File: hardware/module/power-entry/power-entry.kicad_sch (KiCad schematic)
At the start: 19 parts

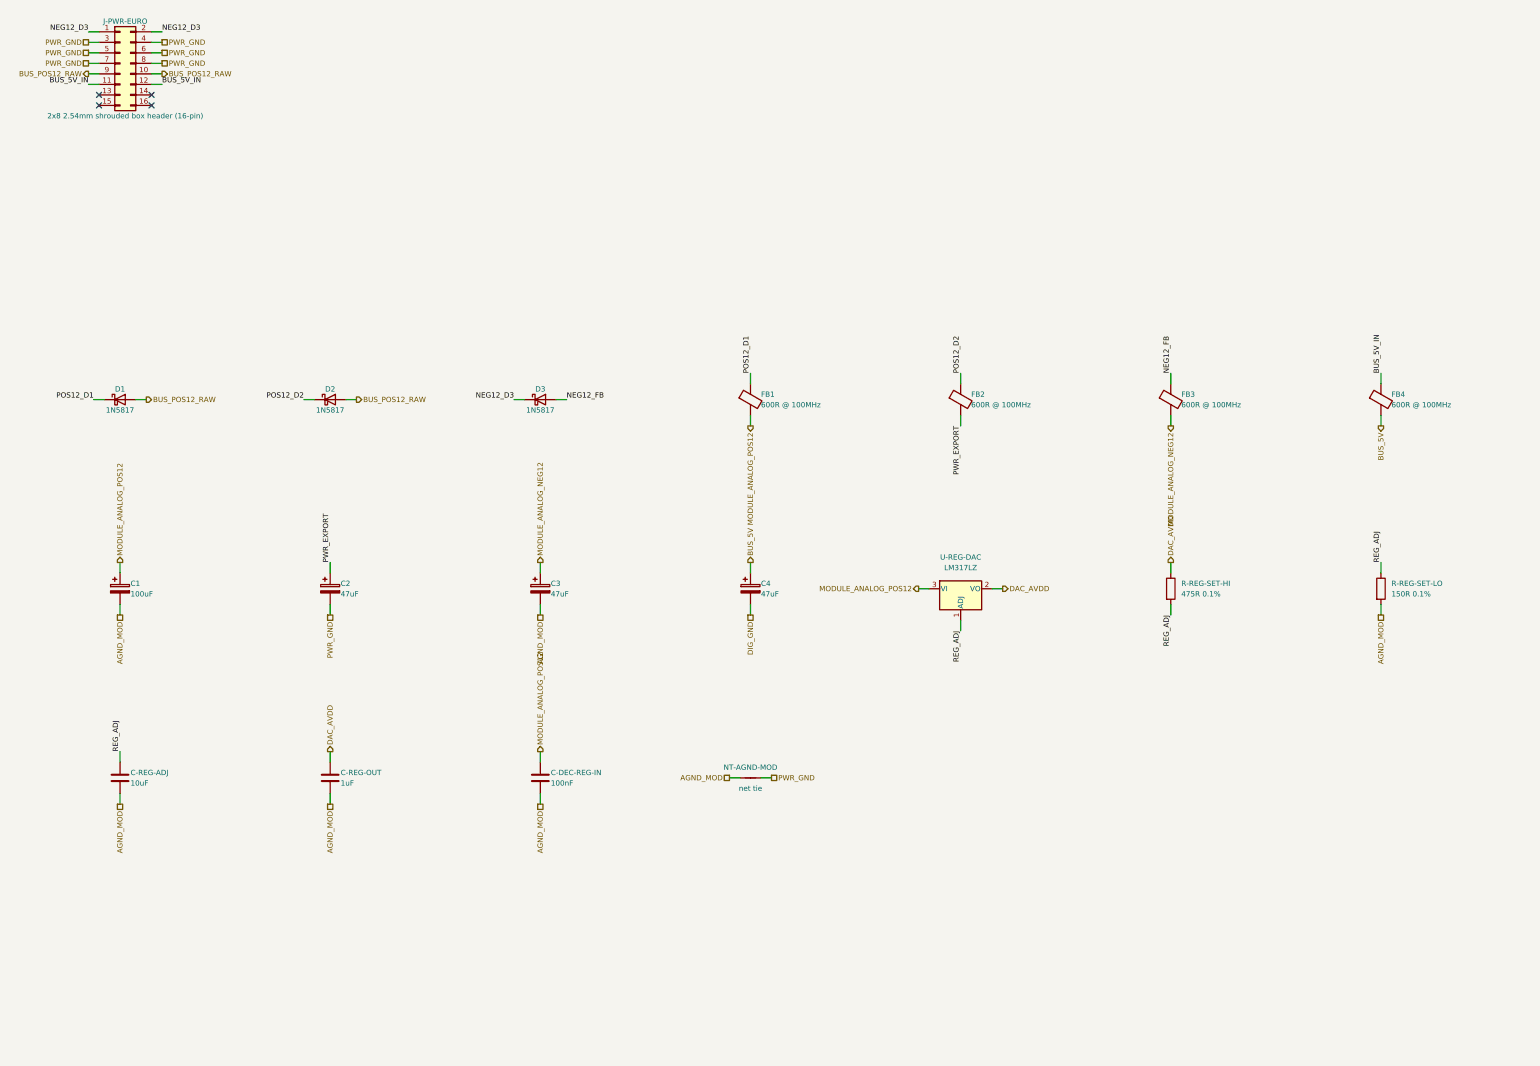
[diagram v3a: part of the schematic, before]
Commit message: Module: four-layer ground settled, local 5 V, metal standoffs, pitch budget, board-to-board header
Owner decisions of 2026-09-30 applied. dig-gnd-topology settled: one star at
J-PWR-EURO's ground pins, DIG_GND a layer-2 plane tied there by the new
NT-DIG-MOD, AGND_MOD its own region by NT-AGND-MOD, PWR_GND on layer 4; the
proposal's bridge under the DAC dropped per SBAS430E p.49 (DIG_GND was an
island tied only through the cable before). PCB-MODULE four layers, the jack
board two. The bus +5 V is not used: U-REG-LOGIC (ADP7118AUJZ-5.0, banked)
makes LOGIC_5V from the analog +12 V; FB4/C4 gone, the 16-pin header kept
with its +5 V/CV/Gate pins no-connect (ADR 0023 point 3 amended). Metal
standoffs: pads AGND_MOD on the jack board, no net on the main board.
pitch-cents-budget settled at 0.76 cents linear / 0.45 RSS from one table.
J-B2B-MOD is Samtec TSW-110-09-G-D. Module sims are stale and re-run next.

Co-Authored-By: Claude Opus 5.5 <noreply@anthropic.com>
Claude-Session: https://claude.ai/code/session_01LmB4muFXnoLprWX4JzuJ5A
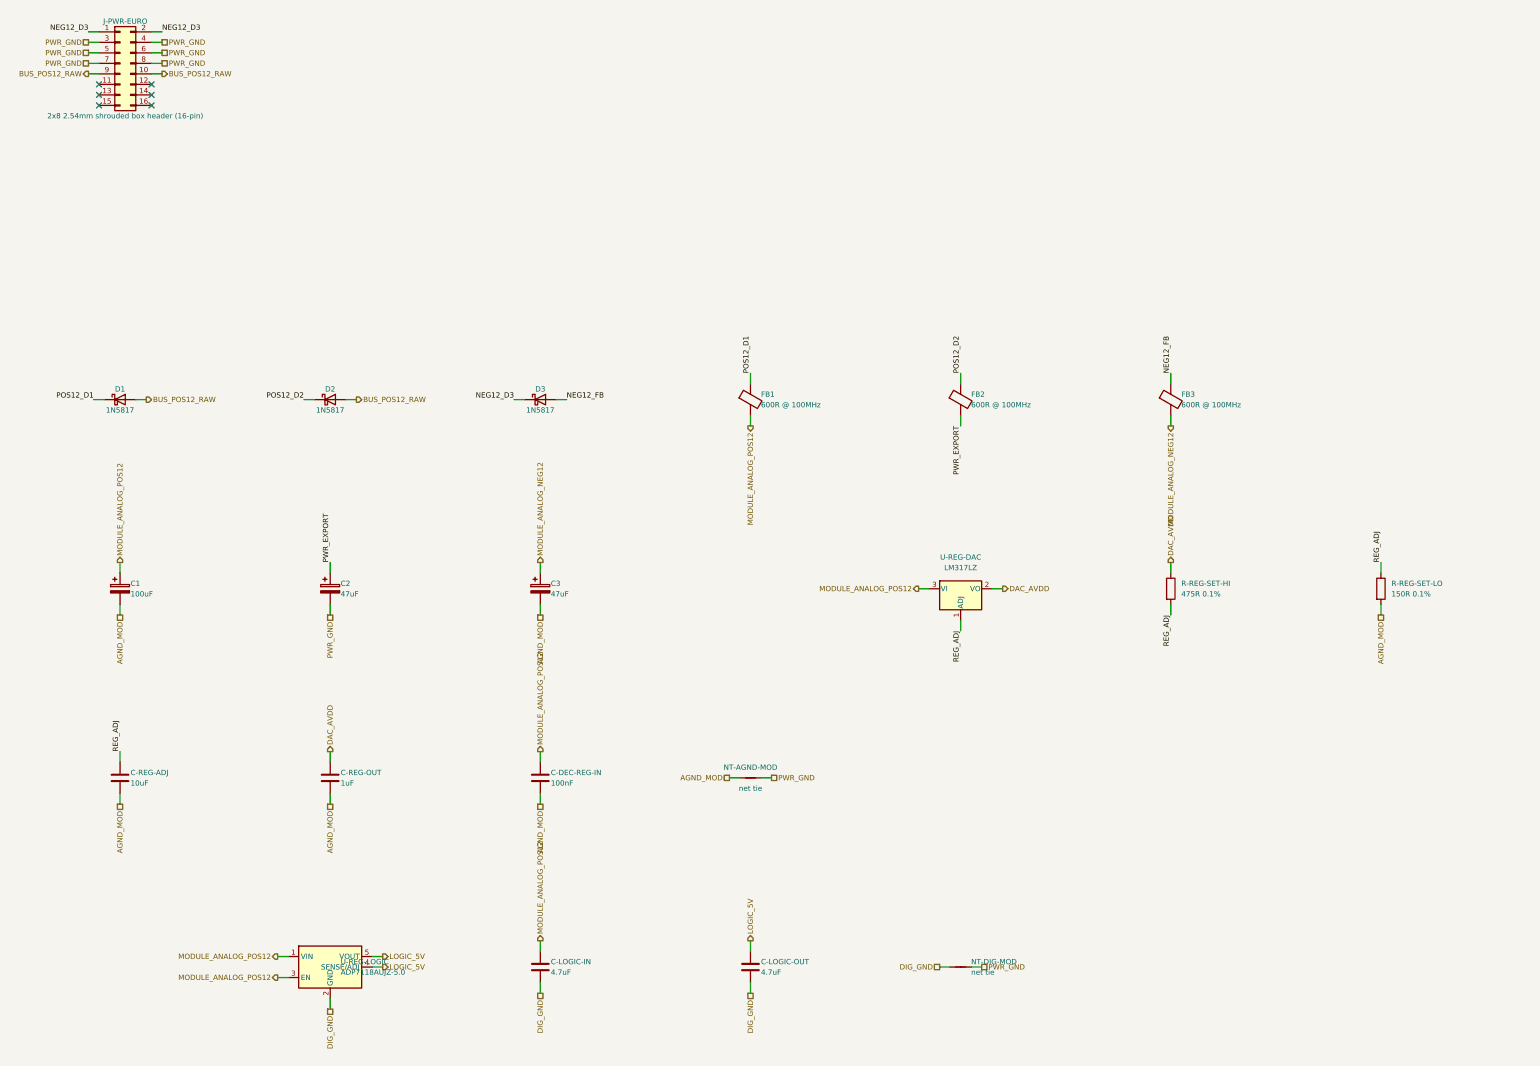
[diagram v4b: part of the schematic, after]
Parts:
- removed C4: 47uF, Capacitor_THT:CP_Radial_D5.0mm_P2.00mm, symbol Device:C_Polarized
- removed FB4: 600R @ 100MHz, Inductor_SMD:L_1206_3216Metric, symbol Device:FerriteBead
- added C-LOGIC-IN, C-LOGIC-OUT: 4.7uF, Capacitor_SMD:C_1206_3216Metric, symbol Device:C
- added NT-DIG-MOD: net tie, NetTie:NetTie-2_SMD_Pad0.5mm, symbol Device:NetTie_2
- added U-REG-LOGIC: ADP7118AUJZ-5.0, Package_TO_SOT_SMD:TSOT-23-5, symbol Regulator_Linear:ADP7142AUJZ
- J-PWR-EURO: Note Keyed, but a key does not make a reversed ribbon impossible. The rack's -12 V is the pin-1 pair, the ribbon's red stripe, and reversing it is what D-REVPOL exists for -> Keyed, but a key does not make a reversed ribbon impossible. The rack's -12 V is the pin-1 pair, the ribbon's red stripe, and reversing it is what D-REVPOL exists for. The bus +5 V (11, 12) and CV/Gate (13-16) pins are NOT USED: pads present, no-connect - the module makes its own 5 V (U-REG-LOGIC), and the header stays 2x8 for commonality with every Eurorack power cable (owner, 2026-09-30)
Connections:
- net DIG_GND: now also C-LOGIC-IN.2, C-LOGIC-OUT.2, NT-DIG-MOD.1, U-REG-LOGIC.2 (GND)
- net MODULE_ANALOG_POS12: now also C-LOGIC-IN.1, U-REG-LOGIC.1 (VIN), U-REG-LOGIC.3 (EN)
- net PWR_GND: now also NT-DIG-MOD.2
- net BUS_5V_IN: no longer names the net of J-PWR-EURO.11 (Pin_11)
- net BUS_5V_IN: no longer J-PWR-EURO.12 (Pin_12)
- new net LOGIC_5V: C-LOGIC-OUT.1, U-REG-LOGIC.4 (SENSE/ADJ), U-REG-LOGIC.5 (VOUT)
- no-connect marks 4 -> 6

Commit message: WIP module power entry: rail PTCs, the instrument's isolated supply (U-ISO), ground split
Sheets, exports, BOM rows, banked datasheets (manifest fragment to follow).
The page drawing, ADR 0027, figures and sims are the next commits.

Co-Authored-By: Claude Opus 5.5 <noreply@anthropic.com>
Claude-Session: https://claude.ai/code/session_01LmB4muFXnoLprWX4JzuJ5A
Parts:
- added C-ISO-IN: 4.7uF 50V, Capacitor_SMD:C_1206_3216Metric, symbol Device:C
- added C-ISO-OUT: 100uF 25V, Capacitor_SMD:CP_Elec_6.3x5.8, symbol Device:C_Polarized
- added C-ISO-Y: 1nF, Capacitor_SMD:C_0805_2012Metric, symbol Device:C
- added D4: 1N5817, Diode_THT:D_DO-41_SOD81_P10.16mm_Horizontal, symbol Diode:1N5817
- added FB4: 600R @ 100MHz, Inductor_SMD:L_1206_3216Metric, symbol Device:FerriteBead
- added L-ISO-IN: 22uH, Inductor_SMD:L_Sunlord_SWPA6028S, symbol Device:L
- added NT-UMB-MOD: net tie, NetTie:NetTie-2_SMD_Pad0.5mm, symbol Device:NetTie_2
- added PTC-ISO: MF-MSMF075/33X-2, Fuse:Fuse_1812_4532Metric, symbol Device:Polyfuse
- added PTC-NEG12, PTC-POS12: MF-MSMF020/60-2, Fuse:Fuse_1812_4532Metric, symbol Device:Polyfuse
- added U-ISO: URB2412YMD-15WR3, woody:Converter_DCDC_Mornsun_URB_YMD-15WR3_THT, symbol woody:URB_YMD-15WR3
- C2: value 47uF -> 100uF 50V; footprint Capacitor_THT:CP_Radial_D5.0mm_P2.00mm -> Capacitor_SMD:CP_Elec_6.3x7.7; LCSC C371230 -> (none); MPN NXB25V47M5*11 2.5TP -> UCM1H101MCL1GS; Manufacturer SamYoung -> Nichicon; Note (none) -> U-ISO's input bulk, ACROSS its input (ISO_VIN_POS to ISO_VI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; Row C-BULK-RAIL -> C-ISO-BULK
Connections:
- net BUS_POS12_RAW: now also PTC-ISO.1, PTC-POS12.1; no longer D1.2 (A), D2.2 (A)
- net DIG_GND: now also NT-UMB-MOD.2
- net PWR_GND: now also C-ISO-OUT.2, C-ISO-Y.2, NT-UMB-MOD.1, U-ISO.6 (0V); no longer C2.2, J-PWR-EURO.3 (Pin_3), J-PWR-EURO.4 (Pin_4), J-PWR-EURO.5 (Pin_5), J-PWR-EURO.6 (Pin_6), J-PWR-EURO.7 (Pin_7), J-PWR-EURO.8 (Pin_8), NT-AGND-MOD.2, NT-DIG-MOD.2
- net NEG12_D3 renamed BUS_NEG12_RAW
- net BUS_NEG12_RAW: now also D4.1 (K), PTC-NEG12.1; no longer D3.1 (K)
- net PWR_EXPORT renamed ISO_FB2
- net ISO_FB2: now also L-ISO-IN.1; no longer C2.1
- new net BUS_GND: J-PWR-EURO.3 (Pin_3), J-PWR-EURO.4 (Pin_4), J-PWR-EURO.5 (Pin_5), J-PWR-EURO.6 (Pin_6), J-PWR-EURO.7 (Pin_7), J-PWR-EURO.8 (Pin_8), NT-AGND-MOD.2, NT-DIG-MOD.2
- new net ISO_POS12: C-ISO-OUT.1, U-ISO.4 (+Vo)
- new net ISO_VIN_NEG: C-ISO-IN.2, C2.2, FB4.2, U-ISO.2 (GND)
- new net ISO_VIN_POS: C-ISO-IN.1, C-ISO-Y.1, C2.1, L-ISO-IN.2, U-ISO.3 (Vin)
- new net NEG12_D4: D4.2 (A), FB4.1
- new net NEG12_PTC3: D3.1 (K), PTC-NEG12.2
- new net POS12_PTC1: D1.2 (A), PTC-POS12.2
- new net POS12_PTC2: D2.2 (A), PTC-ISO.2
- no-connect marks 6 -> 8
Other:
- note added: "ADDED 2026-09-30 (ADR 0027): the rail fuses (PTC-POS12, PTC-NEG12), the instrument's isolated supply - PTC-ISO, D2, FB2, L-ISO-IN on the +12 leg, D4, FB4 on the -12 leg, C2 and C-ISO-IN across, U-ISO, C-ISO-OUT, C-ISO-Y - and NT-UMB-MOD. BUS_GND is the Eurorack ground as it arrives, the star: AGND_MOD (NT-AGND-MOD) and DIG_GND (NT-DIG-MOD) meet it, and PWR_GND - U-ISO's isolated return - meets DI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"

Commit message: ADR 0027 follow-through: load switch page and sheet on ISO_POS12, ADR 0004/0005 amendments, sims re-run, renders
The load switch page states its new supply and the margins it gains (ON
turn-on 0.94 V below U-ISO's floor, was 0.7 V below the bus's); sheet notes
and text follow; the power-entry sheet no longer declares foreign parts its
drawing stopped showing. ADR 0004 and 0005 carry dated amendments pointing
at ADR 0027; pitch-stage.md's exclusion reads as removed. Sim READMEs record
the ground-shift decks and the LM317L model's non-convergence at the fuse's
post-trip 6 ohm. All gates pass; sims re-run on the final netlists.

Co-Authored-By: Claude Opus 5.5 <noreply@anthropic.com>
Claude-Session: https://claude.ai/code/session_01LmB4muFXnoLprWX4JzuJ5A
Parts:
- C1: Note 100uF on +12 V, NOT 47uF - the other three are 47uF and thi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 -> 100uF on +12 V, NOT 47uF - C3 on -12 V is 47uF and this one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
- D2: Note Reverse protection, EXPORTED +12 V branch. Separate from D1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 -> Reverse protection, the +12 V leg of U-ISO's input (ADR 002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
- D3: Note Reverse protection, -12 V branch. CATHODE TO THE BUS, anode to the module's -12 V rail: the rail's current flows out of the module into the bus's -12 V, so this is the one entry diode the other way round from D1/D2 -> Reverse protection, -12 V branch. CATHODE TO THE BUS, anode to the module's -12 V rail: the rail's current flows out of the module into the bus's -12 V, so this is, with D4, the entry diode the other way round from D1/D2
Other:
- note added: "ADDED 2026-09-30 (ADR 0027): the rail fuses (PTC-POS12, PTC-NEG12), the instrument's isolated supply - PTC- ISO, D2, FB2, L-ISO-IN on the +12 leg, D4, FB4 on the -12 leg, C2 and C-ISO-IN across, U-ISO, C-ISO-OUT, C-ISO-Y - and NT-UMB-MOD. BUS_GND is the Eurorack ground as it arrives, the star: AGND_MOD (NT-AGND-MOD) and DIG_GND (NT-DIG-MOD) meet it, and PWR_GND - U-ISO's isolated return - meets D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"
- note added: "FROM THE HAND-WRITTEN NETLIST THIS SHEET REPLACES (verbatim; the part notes are on each part's Note field): AUTHORITATIVE for connectivity. The drawing in power-entry.md is a representation of this file. SCOPE. This circuit owns the rail entry and its fuses, the bead-and-bulk branches, the LM317, the logic 5 V and the instrument's isolated supply up to ISO_POS12 and PWR_GND. The load switch those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"
- note removed: "ADDED 2026-09-30 (ADR 0027): the rail fuses (PTC-POS12, PTC-NEG12), the instrument's isolated supply - PTC-ISO, D2, FB2, L-ISO-IN on the +12 leg, D4, FB4 on the -12 leg, C2 and C-ISO-IN across, U-ISO, C-ISO-OUT, C-ISO-Y - and NT-UMB-MOD. BUS_GND is the Eurorack ground as it arrives, the star: AGND_MOD (NT-AGND-MOD) and DIG_GND (NT-DIG-MOD) meet it, and PWR_GND - U-ISO's isolated return - meets DI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"
- note removed: "FROM THE HAND-WRITTEN NETLIST THIS SHEET REPLACES (verbatim; the part notes are on each part's Note field): AUTHORITATIVE for connectivity. The drawing in power-entry.md is a representation of this file. SCOPE. That drawing shows the whole load switch - LT1641, R-ILIM, the timer and gate capacitors, the FB divider and Q-LOADSW - so the export path can be read in one place. THOSE ARE module/umbili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"
- note removed: "PARTS THIS PAGE'S DRAWING SHOWS AND THIS CIRCUIT DOES NOT OWN - netlist.yaml `foreign:`, exported from the FOREIGN lines below. Each is counted, netted and ordered by its owner; declaring it keeps the drawing checkable (tools/check-netlist.py). FOREIGN R-ILIM: owner module/umbilical-load-switch, row R-ILIM FOREIGN R-GATE-SER: owner module/umbilical-load-switch, row R-GATE-SER FOREIGN R-GATE-COMP: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"

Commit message: U-ISO becomes RECOM RP20-2412SAW: footprint, symbol, sheet, BOM rows
Same land pattern as the MORNSUN part, RECOM's pin numbers; the plain SAW
has no CTRL or Trim pin, so pads 1/2/4/6 and no no-connects. Filter parts'
provenance moved to the RECOM datasheet; PTC-ISO is RECOM's required
input fuse. Page and ADR follow in the next commit.

Co-Authored-By: Claude Opus 5.5 <noreply@anthropic.com>
Claude-Session: https://claude.ai/code/session_01LmB4muFXnoLprWX4JzuJ5A
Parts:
- C-ISO-IN: Note Across U-ISO's input pins, beside them: the ceramic half of the input filter (the datasheet's C1/C2, 4.7uF/50V, p.5 Fig.3) -> Across U-ISO's input pins, beside them: the ceramic half of the input filter (RECOM's Class B C1 for the RP20-24xxSAW, 4.7uF MLCC, PD-6; 50 V here because it sits across both rails)
- C-ISO-OUT: Note U-ISO's output capacitor, the datasheet's Cout 100uF/25V (p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 -> U-ISO's output capacitor, 100uF/25V: well inside the RP20-2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
- C-ISO-Y: Note Across the isolation barrier AT the converter, ISO_VIN_POS to PWR_GND: gives the switching common-mode current a 1 nF path home beside U-ISO instead of round the star and the ribbon (the datasheet's CY, p.5 Fig.3). On the +12 V side so PTC-ISO covers it if it fails short -> Across the isolation barrier AT the converter, ISO_VIN_POS to PWR_GND: gives the switching common-mode current a 1 nF path home beside U-ISO instead of round the star and the ribbon (RECOM's Class B filter puts 470pF across the barrier on each side, C4/C5, PD-6; one 1 nF here). On the +12 V side so PTC-ISO covers it if it fails short
- C2: Note U-ISO's input bulk, ACROSS its input (ISO_VIN_POS to ISO_VIN_NEG, 24 V): the datasheet's Cin, 100uF/50V (MORNSUN-URB_YMD-15WR3.pdf p.4 Fig.2). An electrolytic with real ESR, because it damps L-ISO-IN (power-entry.md) -> U-ISO's input bulk, ACROSS its input (ISO_VIN_POS to ISO_VIN_NEG, 24 V): the external input electrolytic RECOM asks for (RECOM-RP20-AW.pdf PD-5 Note 11, which suggests 220uF/100V where a surge test applies; 100uF/50V here, on the rack's rails). An electrolytic with real ESR, because it damps L-ISO-IN (power-entry.md)
- PTC-ISO: Note The converter branch's fuse, in its +12 V leg ahead of D2: 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 -> The converter branch's fuse, in its +12 V leg ahead of D2, 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
- U-ISO: value URB2412YMD-15WR3 -> RP20-2412SAW; footprint woody:Converter_DCDC_Mornsun_URB_YMD-15WR3_THT -> woody:Converter_DCDC_RECOM_RP20-xxxxSAW_THT; symbol woody:URB_YMD-15WR3 -> woody:RP20-xxxxSAW; MPN URB2412YMD-15WR3 -> RP20-2412SAW; Manufacturer MORNSUN -> RECOM; Note THE INSTRUMENT'S SUPPLY, ISOLATED (ADR 0027): input across the rack's +12 V and -12 V, so the instrument's current loops rail to rail and never enters the rack's ground; output +12 V to the load switch, return on PWR_GND, which meets the module's grounds only through NT-UMB-MOD and NT-DIG-MOD. Ctrl open = on, Trim open = 12 V (p.2, p.5) -> THE INSTRUMENT'S SUPPLY, ISOLATED (ADR 0027): input across the rack's +12 V and -12 V, so the instrument's current loops rail to rail and never enters the rack's ground; output +12 V to the load switch, return on PWR_GND, which meets the module's grounds only through NT-UMB-MOD and NT-DIG-MOD. The standard RP20-2412SAW has no CTRL and no Trim pin (PD-1 Note 3): always on, 12 V nominal. RECOM requires an input fuse (PD-4 Note 8): PTC-ISO; Pins CTRL=1(Ctrl) GND=2(GND) VIN=3(Vin) VO=4(+Vo) TRIM=5(Trim) 0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 -> VIN=1(+Vin) GND=2(-Vin) VO=4(+Vout) 0V=6(-Vout); Pins_source datasheets/discrete-and-power/MORNSUN-URB_YMD-15WR3.pdf p.6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 -> datasheets/discrete-and-power/RECOM-RP20-AW.pdf PD-6 Pinnin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
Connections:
- net ISO_VIN_POS: now also U-ISO.1 (+Vin); no longer U-ISO.3 (Vin)
- no-connect marks 8 -> 6
